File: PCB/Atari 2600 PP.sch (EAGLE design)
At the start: 16 parts, among them U1A SN74AHCT125N, U2A SN74AHCT125N, U3A SN74AHCT125N

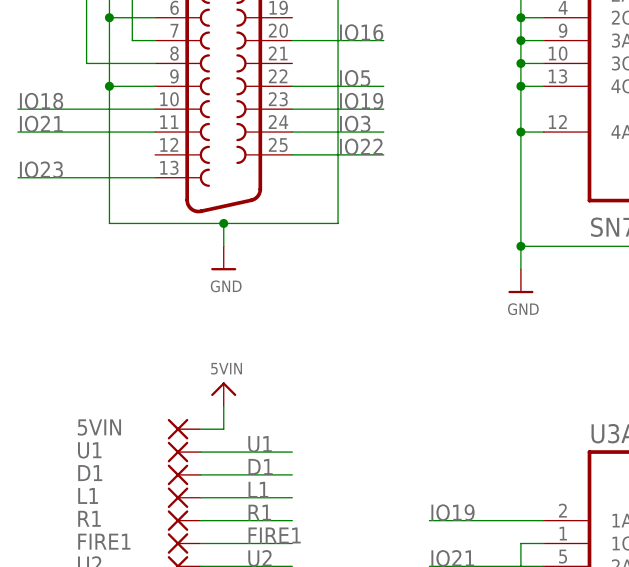
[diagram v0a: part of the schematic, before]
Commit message: Added exposed GND plane at DB25 anchors
All PCBs have been update to have exposed GND plane pads for the DB25 anchor points.

This resolves Issue 54
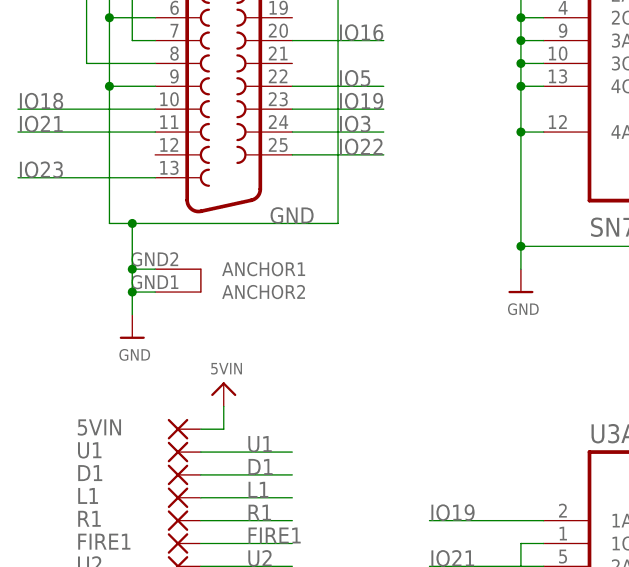
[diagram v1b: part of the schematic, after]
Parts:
- X1: device SparkFun-Retired:DB25_FEMALEH -> SparkFun-Retired:DB25_FEMALEHP
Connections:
- net GND: now also X1.ANCHOR1, X1.ANCHOR2
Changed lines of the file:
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@@
 </classes>
 <parts>
-<part name="X1" library="SparkFun-Retired" deviceset="DB25_FEMALE" device="H"/>
+<part name="X1" library="SparkFun-Retired" deviceset="DB25_FEMALE" device="HP"/>
 <part name="U$44" library="microbuilder" deviceset="VIN" device="" value="5VIN"/>
 <part name="U$45" library="Airquality_Sensor" library_urn="urn:adsk.eagle:library:16015176" deviceset="GND" device=""/>
@@
 <attribute name="VALUE" x="227.076" y="-65.024" size="1.27" layer="96"/>
 </instance>
-<instance part="U$45" gate="G$1" x="238.76" y="-114.3" smashed="yes">
-<attribute name="VALUE" x="237.236" y="-116.84" size="1.27" layer="96"/>
+<instance part="U$45" gate="G$1" x="228.6" y="-121.92" smashed="yes">
+<attribute name="VALUE" x="227.076" y="-124.46" size="1.27" layer="96"/>
 </instance>
 <instance part="U3A" gate="G$1" x="292.1" y="-152.4" smashed="yes">
@@
 <nets>
 <net name="GND" class="0">
-<segment>
-<pinref part="U$45" gate="G$1" pin="GND"/>
-<wire x1="251.46" y1="-109.22" x2="238.76" y2="-109.22" width="0.1524" layer="91"/>
-<wire x1="238.76" y1="-109.22" x2="238.76" y2="-111.76" width="0.1524" layer="91"/>
-<junction x="238.76" y="-109.22"/>
-<wire x1="238.76" y1="-109.22" x2="226.06" y2="-109.22" width="0.1524" layer="91"/>
-<wire x1="226.06" y1="-81.28" x2="226.06" y2="-83.82" width="0.1524" layer="91"/>
-<wire x1="226.06" y1="-83.82" x2="226.06" y2="-86.36" width="0.1524" layer="91"/>
-<wire x1="226.06" y1="-86.36" x2="226.06" y2="-93.98" width="0.1524" layer="91"/>
-<wire x1="226.06" y1="-93.98" x2="226.06" y2="-109.22" width="0.1524" layer="91"/>
-<pinref part="X1" gate="-1" pin="9"/>
-<wire x1="251.46" y1="-78.74" x2="251.46" y2="-109.22" width="0.1524" layer="91"/>
-<wire x1="231.14" y1="-93.98" x2="226.06" y2="-93.98" width="0.1524" layer="91"/>
-<junction x="226.06" y="-93.98"/>
-<pinref part="X1" gate="-1" pin="6"/>
-<wire x1="231.14" y1="-86.36" x2="226.06" y2="-86.36" width="0.1524" layer="91"/>
-<junction x="226.06" y="-86.36"/>
-<pinref part="X1" gate="-1" pin="5"/>
-<wire x1="231.14" y1="-83.82" x2="226.06" y2="-83.82" width="0.1524" layer="91"/>
-<junction x="226.06" y="-83.82"/>
-<pinref part="X1" gate="-1" pin="4"/>
-<wire x1="231.14" y1="-81.28" x2="226.06" y2="-81.28" width="0.1524" layer="91"/>
-<pinref part="X1" gate="-1" pin="16"/>
-<wire x1="246.38" y1="-78.74" x2="251.46" y2="-78.74" width="0.1524" layer="91"/>
-<pinref part="X1" gate="-1" pin="3"/>
-<wire x1="231.14" y1="-78.74" x2="226.06" y2="-78.74" width="0.1524" layer="91"/>
-<wire x1="226.06" y1="-78.74" x2="226.06" y2="-81.28" width="0.1524" layer="91"/>
-<junction x="226.06" y="-81.28"/>
-</segment>
 <segment>
 <pinref part="U$46" gate="G$1" pin="GND"/>
@@
 <wire x1="236.22" y1="-165.1" x2="238.76" y2="-165.1" width="0.1524" layer="91"/>
 </segment>
+<segment>
+<wire x1="251.46" y1="-109.22" x2="228.6" y2="-109.22" width="0.1524" layer="91"/>
+<wire x1="228.6" y1="-109.22" x2="226.06" y2="-109.22" width="0.1524" layer="91"/>
+<wire x1="226.06" y1="-81.28" x2="226.06" y2="-83.82" width="0.1524" layer="91"/>
+<wire x1="226.06" y1="-83.82" x2="226.06" y2="-86.36" width="0.1524" layer="91"/>
+<wire x1="226.06" y1="-86.36" x2="226.06" y2="-93.98" width="0.1524" layer="91"/>
+<wire x1="226.06" y1="-93.98" x2="226.06" y2="-109.22" width="0.1524" layer="91"/>
+<pinref part="X1" gate="-1" pin="9"/>
+<wire x1="251.46" y1="-78.74" x2="251.46" y2="-109.22" width="0.1524" layer="91"/>
+<wire x1="231.14" y1="-93.98" x2="226.06" y2="-93.98" width="0.1524" layer="91"/>
+<junction x="226.06" y="-93.98"/>
+<pinref part="X1" gate="-1" pin="6"/>
+<wire x1="231.14" y1="-86.36" x2="226.06" y2="-86.36" width="0.1524" layer="91"/>
+<junction x="226.06" y="-86.36"/>
+<pinref part="X1" gate="-1" pin="5"/>
+<wire x1="231.14" y1="-83.82" x2="226.06" y2="-83.82" width="0.1524" layer="91"/>
+<junction x="226.06" y="-83.82"/>
+<pinref part="X1" gate="-1" pin="4"/>
+<wire x1="231.14" y1="-81.28" x2="226.06" y2="-81.28" width="0.1524" layer="91"/>
+<pinref part="X1" gate="-1" pin="16"/>
+<wire x1="246.38" y1="-78.74" x2="251.46" y2="-78.74" width="0.1524" layer="91"/>
+<pinref part="X1" gate="-1" pin="3"/>
+<wire x1="231.14" y1="-78.74" x2="226.06" y2="-78.74" width="0.1524" layer="91"/>
+<wire x1="226.06" y1="-78.74" x2="226.06" y2="-81.28" width="0.1524" layer="91"/>
+<junction x="226.06" y="-81.28"/>
+<pinref part="U$45" gate="G$1" pin="GND"/>
+<wire x1="228.6" y1="-119.38" x2="228.6" y2="-116.84" width="0.1524" layer="91"/>
+<junction x="228.6" y="-109.22"/>
+<pinref part="X1" gate="-1" pin="ANCHOR1"/>
+<wire x1="228.6" y1="-116.84" x2="228.6" y2="-114.3" width="0.1524" layer="91"/>
+<wire x1="228.6" y1="-114.3" x2="228.6" y2="-109.22" width="0.1524" layer="91"/>
+<wire x1="231.14" y1="-114.3" x2="228.6" y2="-114.3" width="0.1524" layer="91"/>
+<junction x="228.6" y="-114.3"/>
+<pinref part="X1" gate="-1" pin="ANCHOR2"/>
+<wire x1="231.14" y1="-116.84" x2="228.6" y2="-116.84" width="0.1524" layer="91"/>
+<junction x="228.6" y="-116.84"/>
+<label x="243.84" y="-109.22" size="1.778" layer="95"/>
+</segment>
 </net>
